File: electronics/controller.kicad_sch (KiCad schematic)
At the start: 8 parts, among them J1 Conn_01x02, U1 K7803JT-500R3-LB, U2 LMTOE78_05-0.5

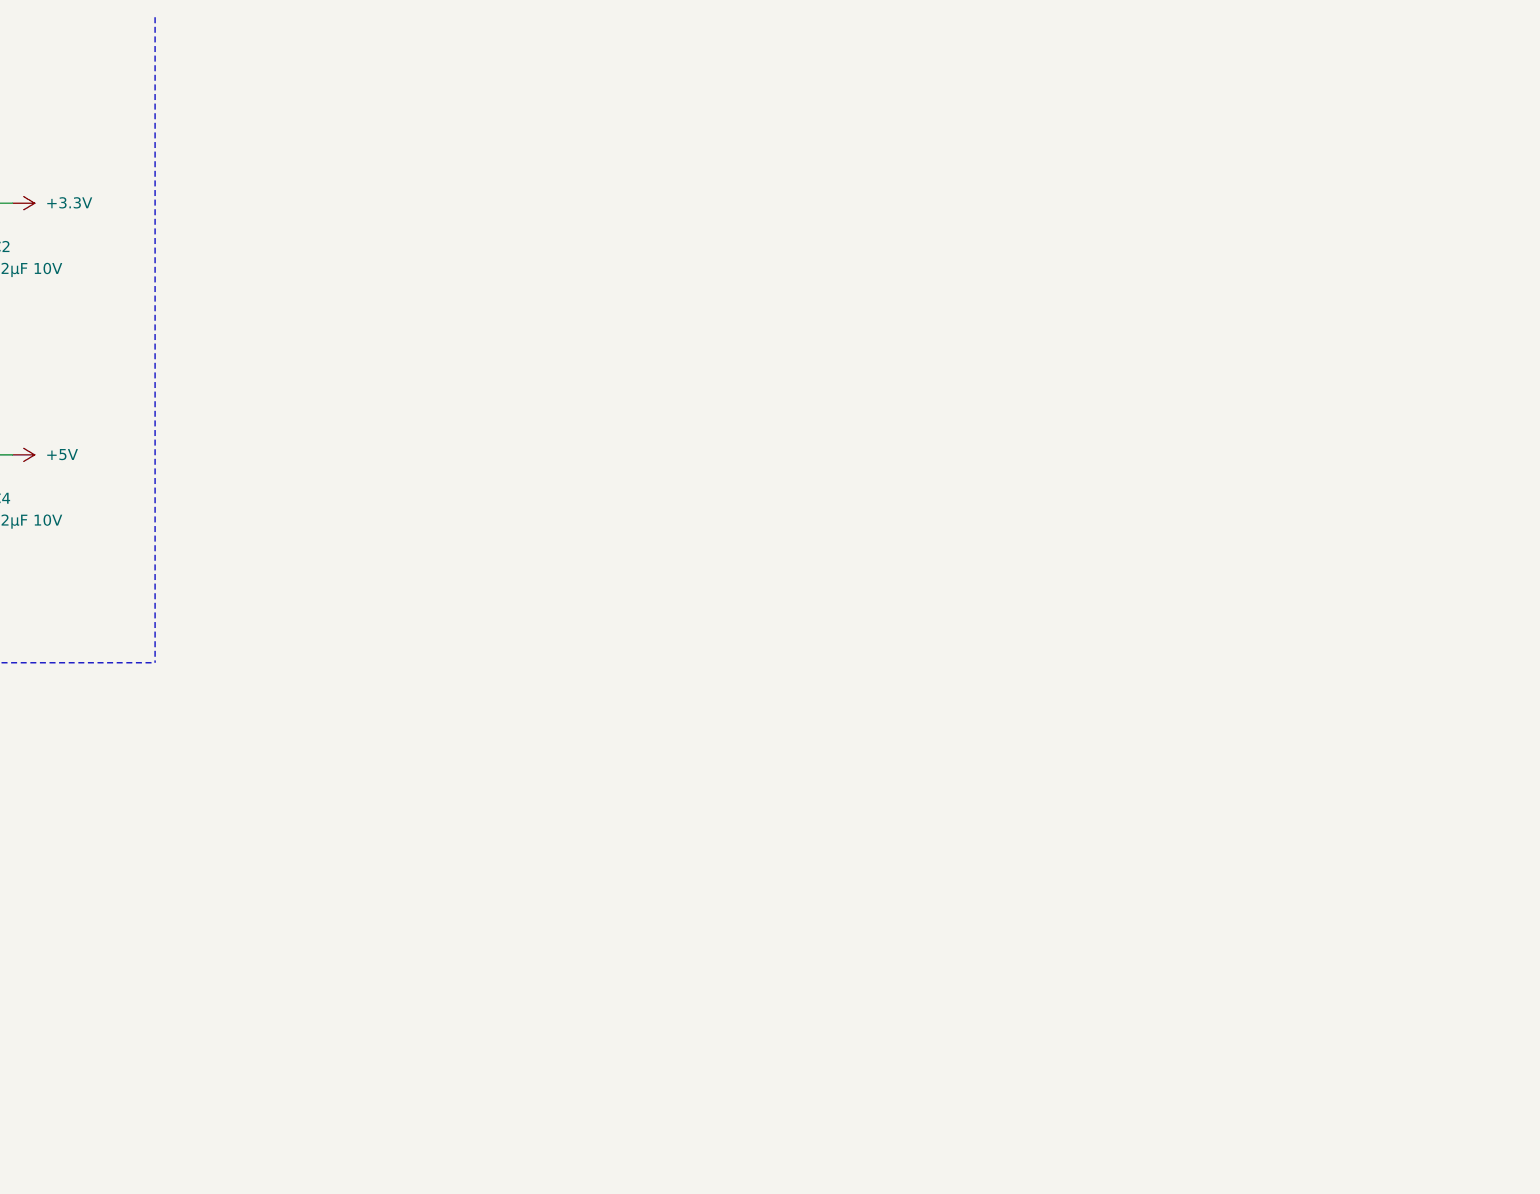
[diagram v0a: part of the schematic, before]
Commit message: ✨ Add the ESP32-S3 microcontroller on KiCad's schematic
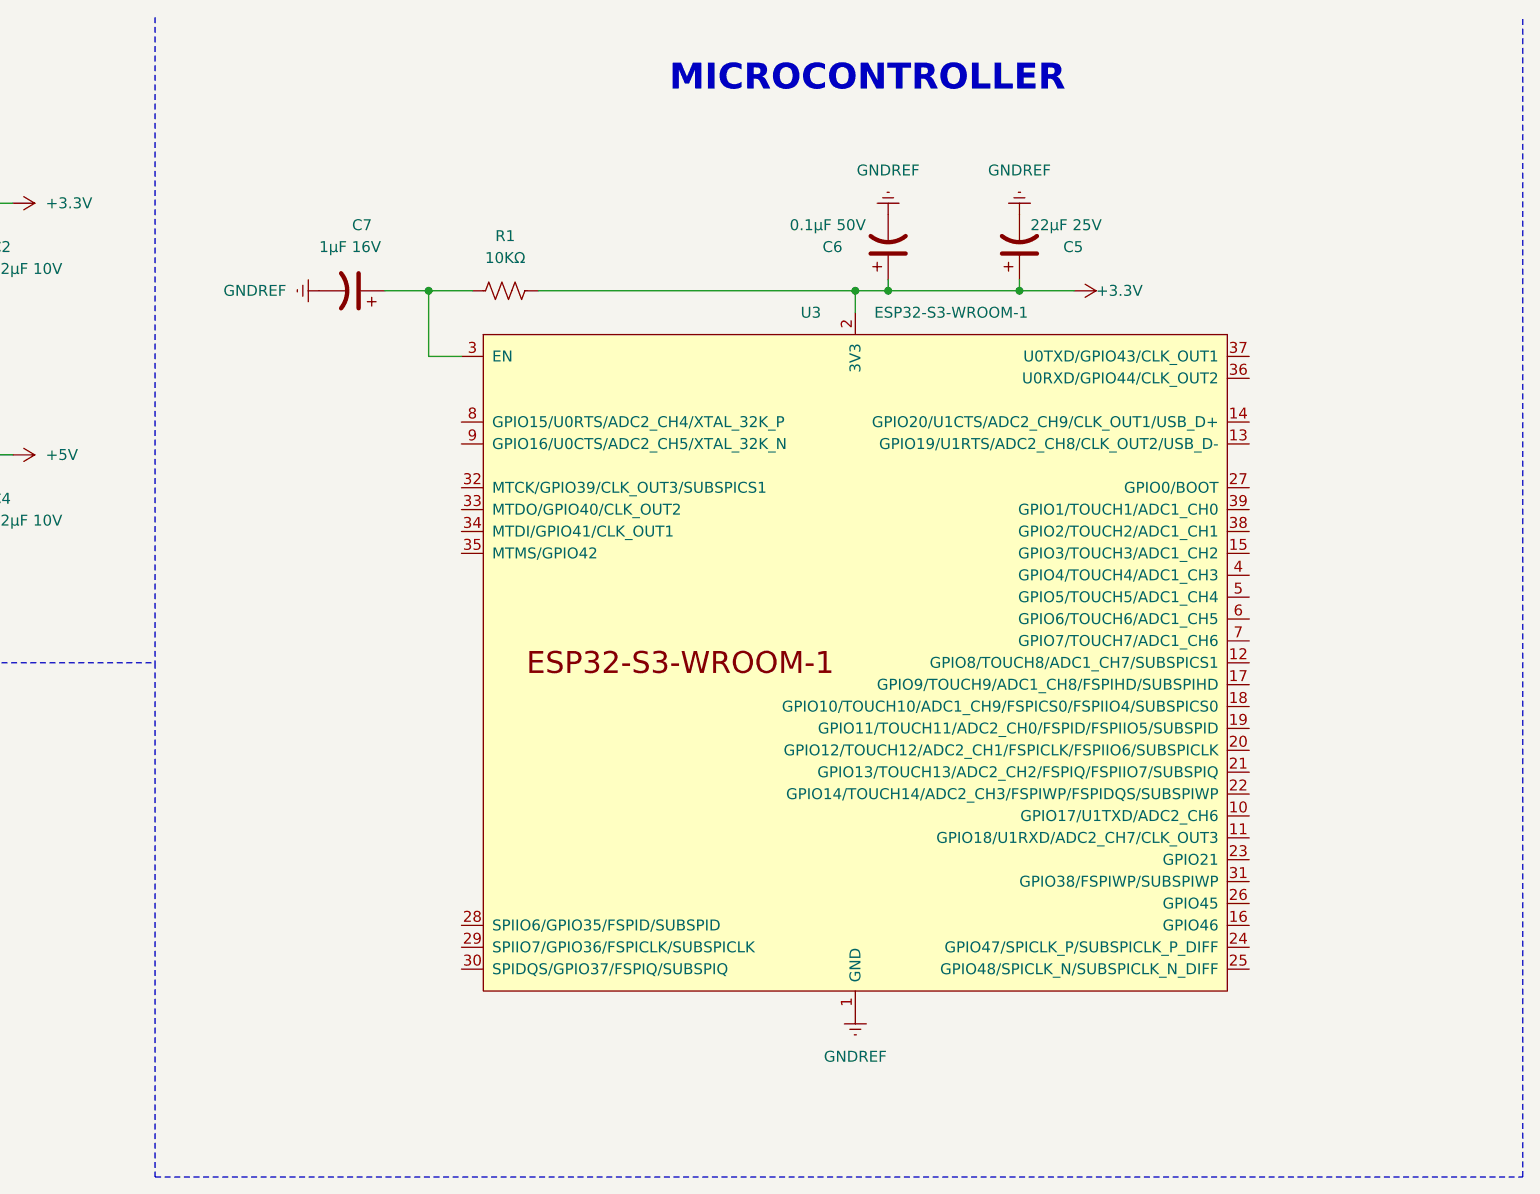
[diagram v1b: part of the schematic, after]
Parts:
- added C5: 22µF 25V, symbol Project:C_Polarized_US
- added C6: 0.1µF 50V, symbol Project:C_Polarized_US
- added C7: 1µF 16V, symbol Project:C_Polarized_US
- added R1: 10KΩ, symbol Project:R_US
- added U3: ESP32-S3-WROOM-1, PCM_Espressif:ESP32-S3-WROOM-1, symbol Project:ESP32-S3-WROOM-1
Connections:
- net +3.3V: now also C5.1, C6.1, R1.2, U3.2 (3V3)
- net GNDREF: now also C5.2, C6.2, C7.2, U3.1 (GND), U3.40 (GND), U3.41 (GND)
- new net: C7.1, R1.1, U3.3 (EN)
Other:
- note added: "MICROCONTROLLER"

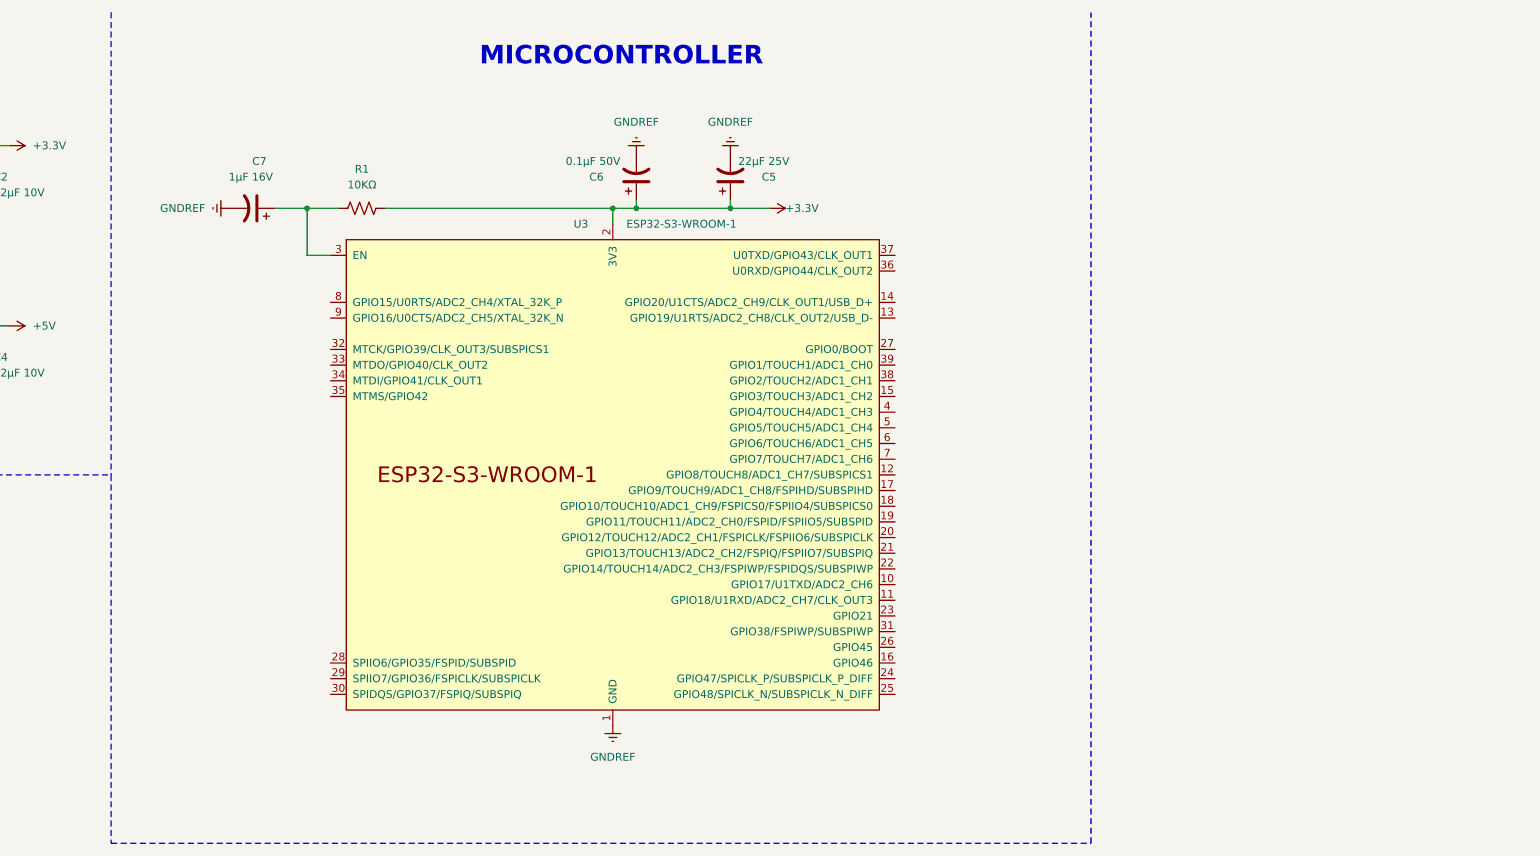
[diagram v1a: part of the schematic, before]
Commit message: ✨ Add EN, Boot and Pause/Resume_Print buttons on KiCad's schematic
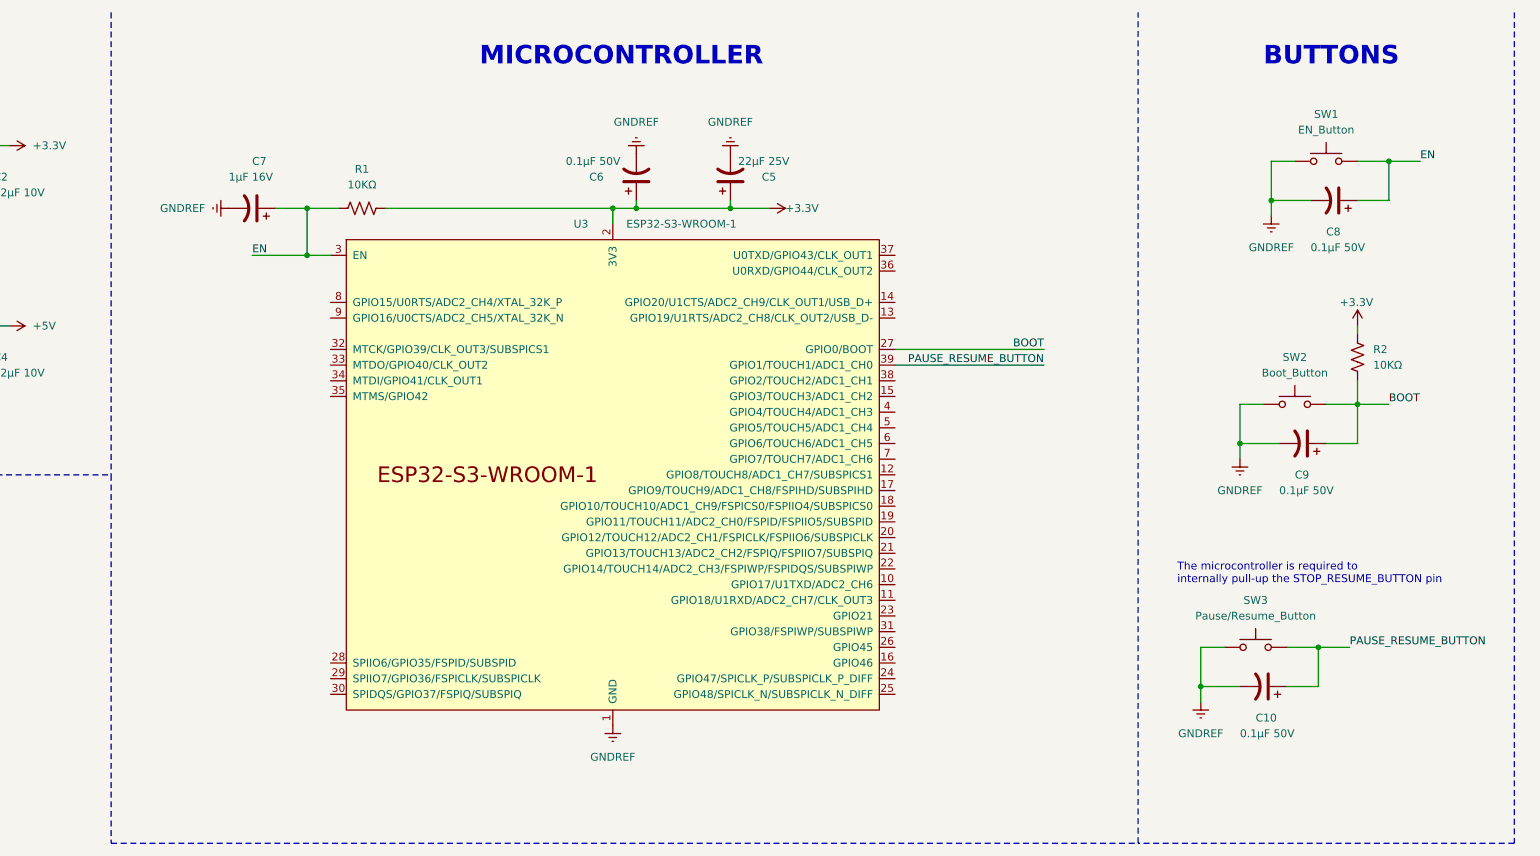
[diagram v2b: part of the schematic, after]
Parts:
- added C10, C8, C9: 0.1µF 50V, symbol Project:C_Polarized_US
- added R2: 10KΩ, symbol Project:R_US
- added SW1: EN_Button, symbol Project:SW_Push
- added SW2: Boot_Button, symbol Project:SW_Push
- added SW3: Pause/Resume_Button, symbol Project:SW_Push
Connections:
- net +3.3V: now also R2.2
- net GNDREF: now also C10.2, C8.2, C9.2, SW1.1, SW2.1, SW3.1
- net EN: now reaches C7.1, R1.1, U3.3 (EN)
- net EN: now also C8.1, SW1.2
- net BOOT: now reaches U3.27 (GPIO0/BOOT)
- net BOOT: now also C9.1, R2.1, SW2.2
- net PAUSE_RESUME_BUTTON: now reaches U3.39 (GPIO1/TOUCH1/ADC1_CH0)
- net PAUSE_RESUME_BUTTON: now also C10.1, SW3.2
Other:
- note added: "BUTTONS"
- note added: "The microcontroller is required to internally pull-up the STOP_RESUME_BUTTON pin"

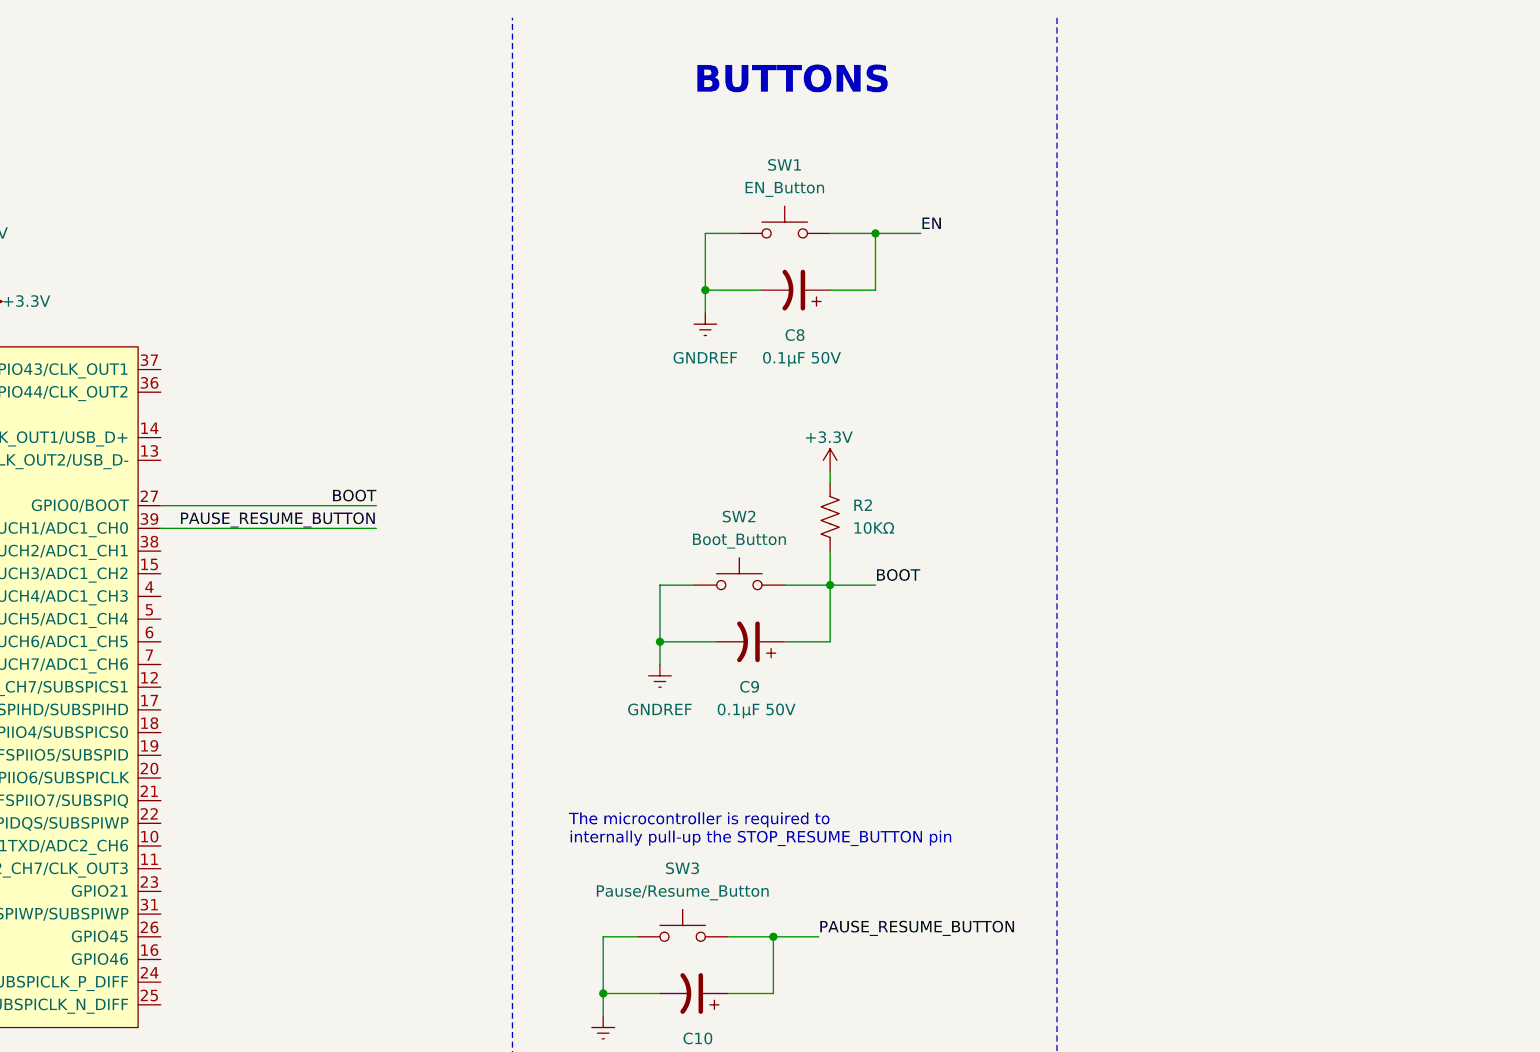
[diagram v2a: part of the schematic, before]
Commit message: ✨ Add X and Y axes endstops on KiCad schematic
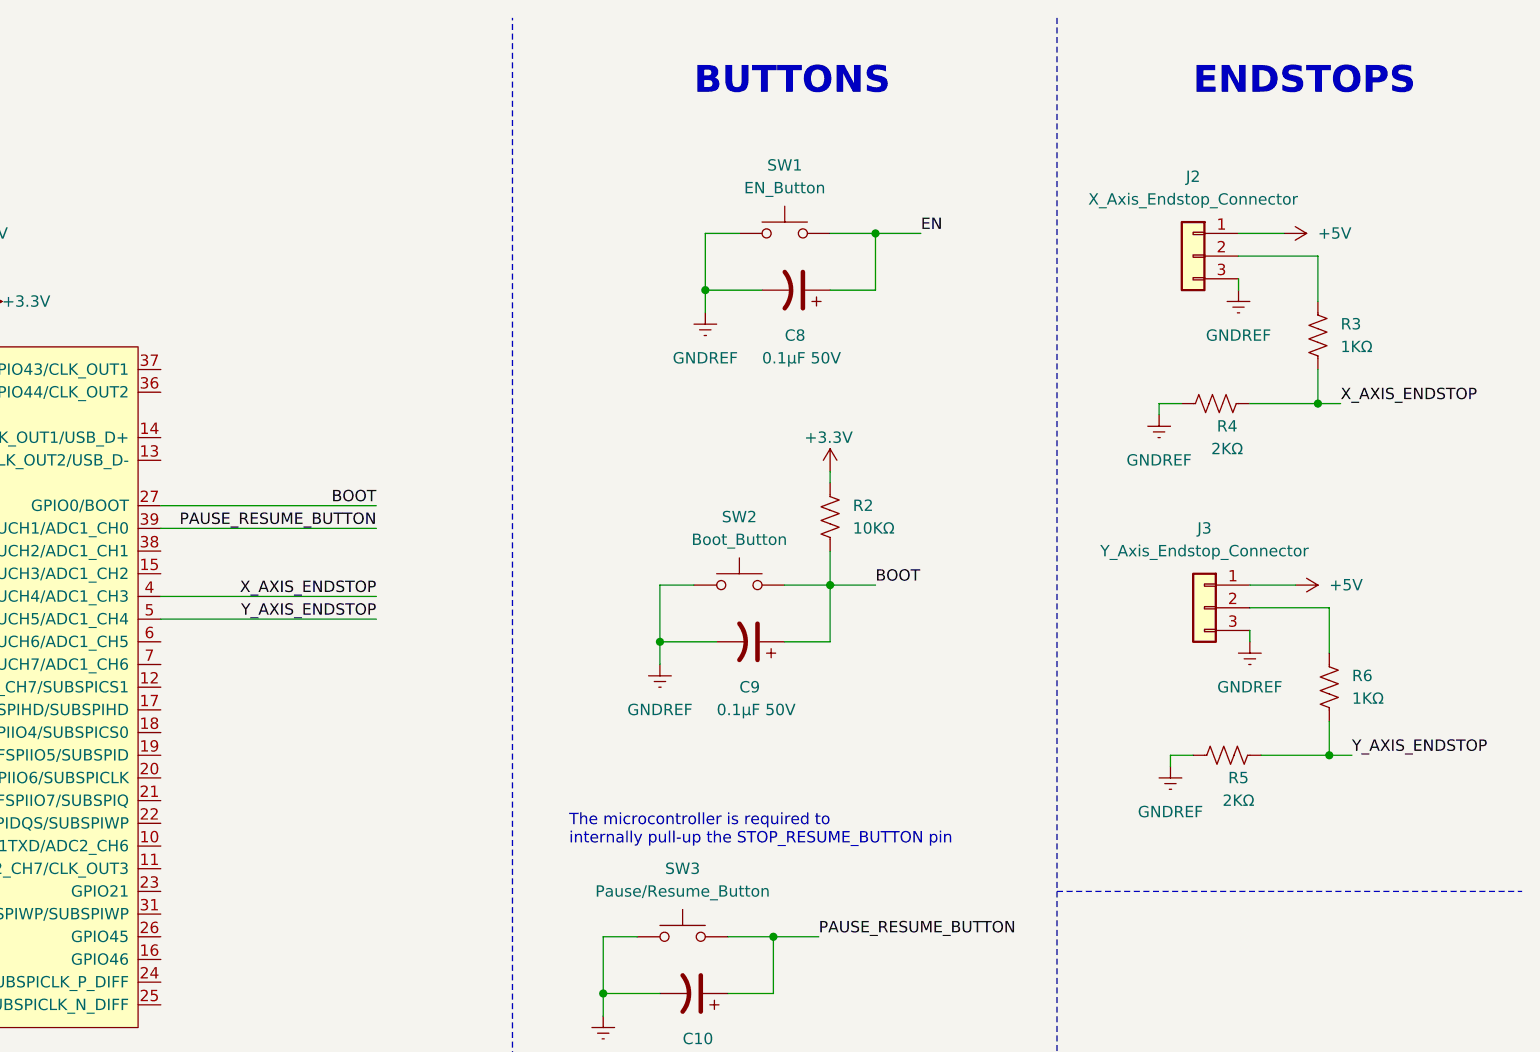
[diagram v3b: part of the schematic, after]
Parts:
- added J2: X_Axis_Endstop_Connector, symbol Project:Conn_01x03
- added J3: Y_Axis_Endstop_Connector, symbol Project:Conn_01x03
- added R3, R6: 1KΩ, symbol Project:R_US
- added R4, R5: 2KΩ, symbol Project:R_US
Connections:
- net +5V: now also J2.1 (Pin_1), J3.1 (Pin_1)
- net GNDREF: now also J2.3 (Pin_3), J3.3 (Pin_3), R4.2, R5.2
- net X_AXIS_ENDSTOP: now reaches U3.4 (GPIO4/TOUCH4/ADC1_CH3)
- net X_AXIS_ENDSTOP: now also R3.1, R4.1
- net Y_AXIS_ENDSTOP: now reaches U3.5 (GPIO5/TOUCH5/ADC1_CH4)
- net Y_AXIS_ENDSTOP: now also R5.1, R6.1
- new net: J3.2 (Pin_2), R6.2
- new net: J2.2 (Pin_2), R3.2
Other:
- note added: "ENDSTOPS"
